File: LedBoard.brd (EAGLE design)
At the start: 100 x 10 mm, 18 parts

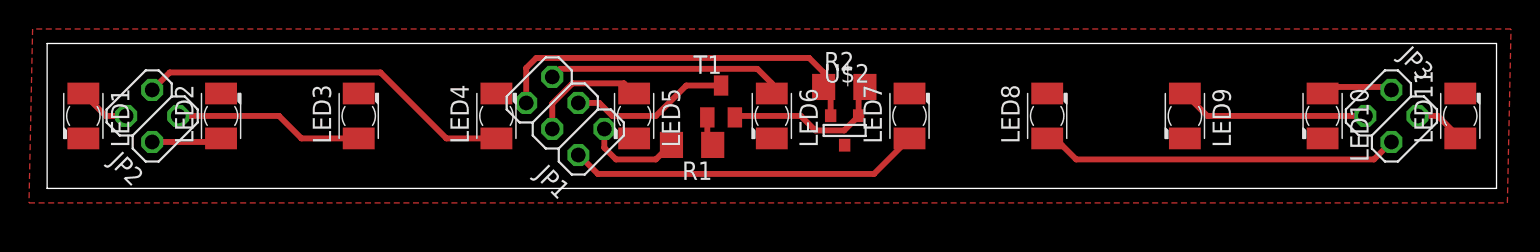
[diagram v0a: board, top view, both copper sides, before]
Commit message: Finished Routing an Panelizing
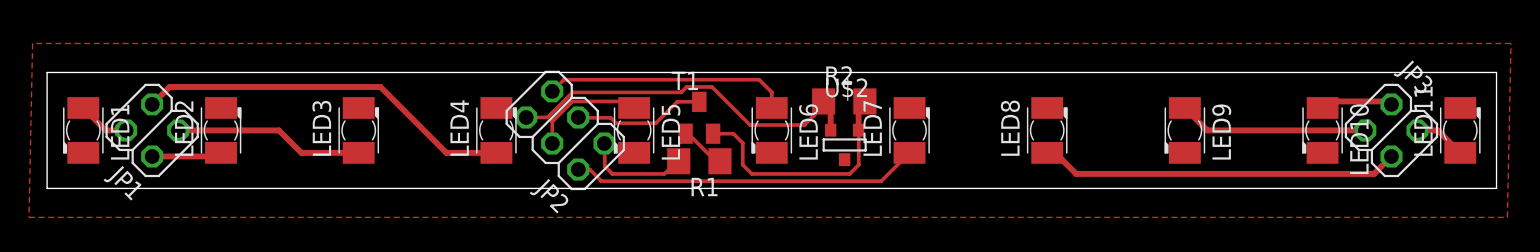
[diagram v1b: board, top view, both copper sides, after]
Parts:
- JP1: device pinhead:2X03 -> pinhead:2X02
- JP2: device pinhead:2X02 -> pinhead:2X03
- moved JP1 28.5 mm to (7.25, 4.00)
- moved JP2 28.5 mm to (35.8, 4.00)
- moved T1 1.88 mm to (45.0, 4.88)
- moved R1 1.23 mm to (45.0, 1.88)
- moved JP3 1.00 mm to (92.8, 4.00)
- moved LED1 1.00 mm to (2.50, 4.00)
- moved LED10 1.00 mm to (88.0, 4.00)
- moved LED11 1.00 mm to (97.5, 4.00)
- moved LED2 1.00 mm to (12.0, 4.00)
- moved LED3 1.00 mm to (21.5, 4.00)
- moved LED4 1.00 mm to (31.0, 4.00)
- moved LED5 1.00 mm to (40.5, 4.00)
- moved LED6 1.00 mm to (50.0, 4.00)
- moved LED7 1.00 mm to (59.5, 4.00)
- moved LED8 1.00 mm to (69.0, 4.00)
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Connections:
- net GND_TRANS: now also JP2.3; no longer JP1.3
- net N$1: now also JP1.4; no longer JP2.4
- net N$14: now also JP2.2; no longer JP1.2
- net N$15: now also JP2.1; no longer JP1.1
- net N$3: now also JP1.2; no longer JP2.2
- net N$4: now also JP1.1; no longer JP2.1
- net N$5: now also JP1.3; no longer JP2.3
- net N$6: now also JP2.4; no longer JP1.4
- net N$7: now also JP2.5; no longer JP1.5
- net N$9: now also JP2.6; no longer JP1.6
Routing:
- net N$2: track 11.6 -> 16.9 mm
- net GND_TRANS: track 11.1 -> 9.12 mm
- net N$15: track 6.68 -> 8.45 mm
- net N$9: track 26.8 -> 25.6 mm
- net N$10: track 2.08 -> 3.31 mm
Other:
- board size 100 x 10 mm -> 100 x 8 mm

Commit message: Changed tolerances on ledboard and mainboard
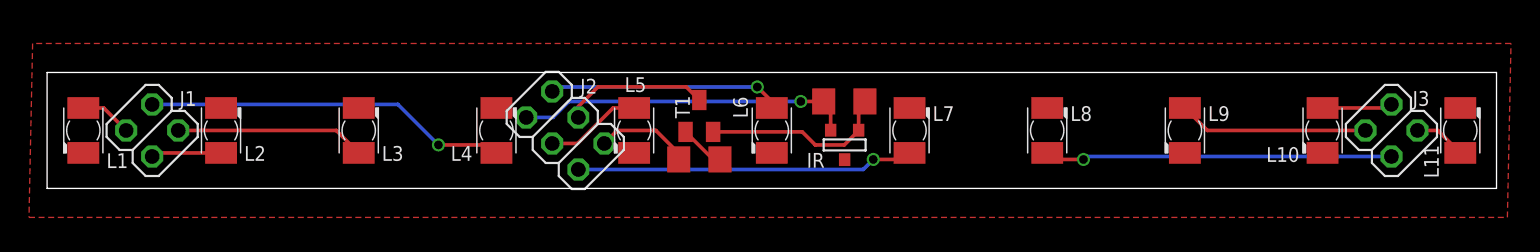
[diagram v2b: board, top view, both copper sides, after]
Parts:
- moved R1 0.12 mm to (45.0, 2.00)
- moved T1 0.12 mm to (45.0, 5.00)
- renumbered JP1 to J1, JP2 to J2, JP3 to J3, LED1 to L1, LED10 to L10, LED11 to L11, LED2 to L2, LED3 to L3, LED4 to L4, LED5 to L5, LED6 to L6, LED7 to L7, LED8 to L8, LED9 to L9, U$2 to IR
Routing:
- net N$2: track 16.9 -> 13.0 mm
- net N$9: track 25.6 -> 23.2 mm, vias 0 -> 1
- net N$6: track 8.74 -> 6.66 mm
- net N$15: track 8.45 -> 6.58 mm
- net N$8: track 4.75 -> 3.60 mm
- net N$5: track 26.1 -> 25.1 mm, vias 0 -> 1
- net GND_TRANS: track 9.12 -> 10.0 mm
- net N$7: track 16.9 -> 16.1 mm, vias 0 -> 1
- net N$13: track 24.8 -> 24.0 mm, vias 0 -> 1
- net N$14: track 24.0 -> 23.3 mm, vias 0 -> 1
